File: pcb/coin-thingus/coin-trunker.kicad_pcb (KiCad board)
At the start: 2 copper layers, 65 x 80.5 mm, 69 parts, among them J1 6P6C, J2 6P6C, J3 Conn_02x20_Odd_Even, J4 Barrel_Jack_Switch_MountingPin, J5 Screw_Terminal_01x02, J6 Conn_01x05, J7 USB_B_Micro, K1 AGQ200A4, K2 AGQ200A4, K3 AGQ200A4, K4 AGQ200A4, Q1 BSS123L, T1 Sumida-13324-TO86, U1 ULN2003LV, U2 LT8304, U3 H11AA1, U4 TCA9534, U5 ILD74, U6 MCP1703A-3302_SOT23, U7 STM32F042F6Px

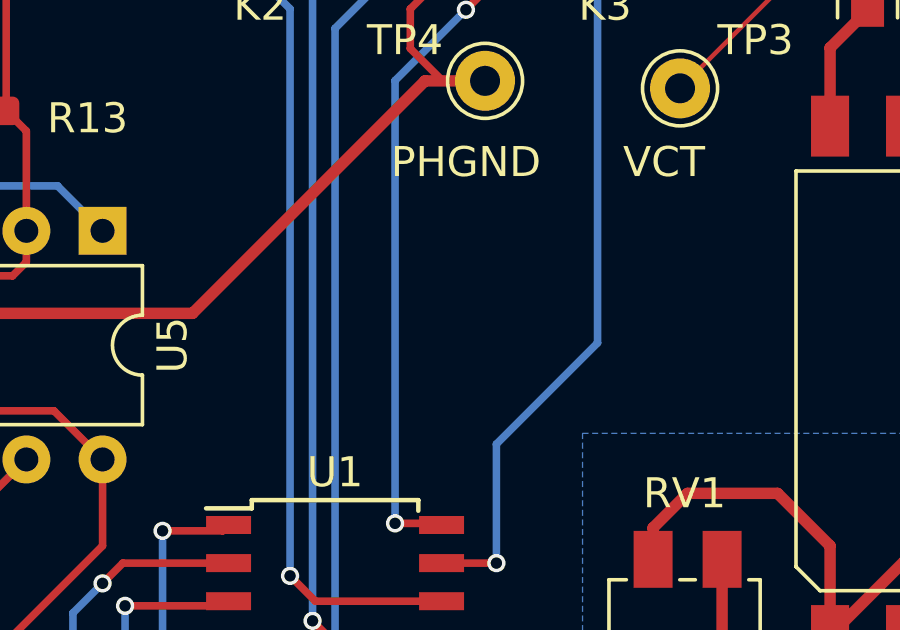
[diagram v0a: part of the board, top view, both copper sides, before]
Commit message: Add CERN-OHL-W v2 license
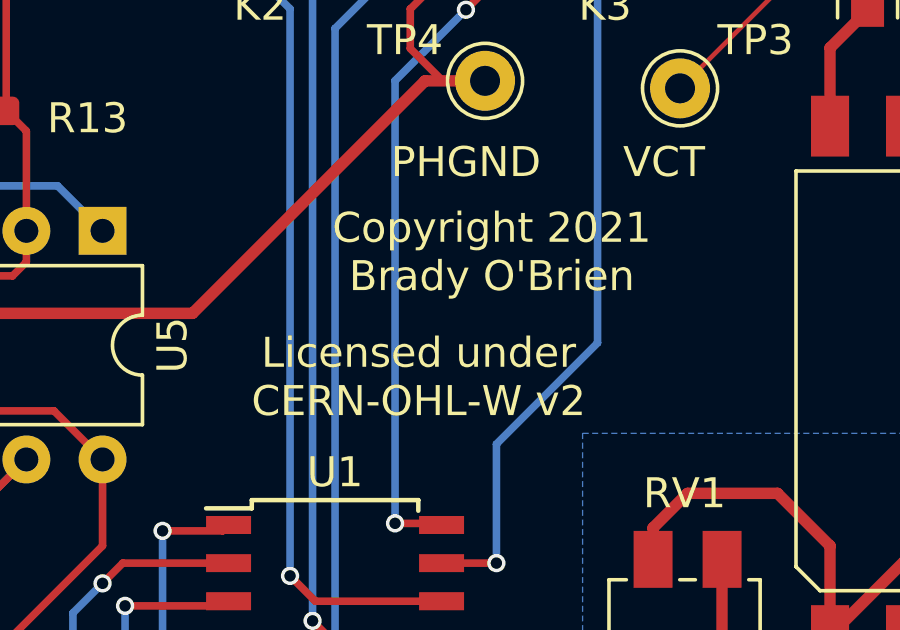
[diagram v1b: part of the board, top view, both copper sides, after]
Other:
- board text added: "Copyright 2021 Brady O'Brien"
- board text added: "Licensed under CERN-OHL-W v2"

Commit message: Some work towards v0.2
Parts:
- removed G***: LOGO, coin-trunker:phone_image
- removed JP1: SolderJumper_2_Open, Jumper:SolderJumper-2_P1.3mm_Open_Pad1.0x1.5mm
- added SW1: SW_SPST, Button_Switch_SMD:SW_SPST_TL3342, F.Cu at (126.3, 83.6)
- added U8: LTV-217, Package_SO:SOP-4_4.4x2.6mm_P1.27mm, F.Cu at (147.3, 67.6)
- K1, K2, K3: value AGQ200A4 -> HFD4/5-S
- R10, R7: footprint Resistor_SMD:R_0612_1632Metric -> Resistor_SMD:R_1206_3216Metric
- U1: footprint Package_SO:SOIC-16W_5.3x10.2mm_P1.27mm -> Package_SO:SOIC-16_3.9x9.9mm_P1.27mm
- U3: value H11AA1 -> LTV-217; footprint Package_DIP:DIP-6_W7.62mm -> Package_SO:SOP-4_4.4x2.6mm_P1.27mm
- U5: value ILD74 -> LTV-217; footprint Package_DIP:DIP-8_W7.62mm -> Package_SO:SOP-4_4.4x2.6mm_P1.27mm
- moved K4 107.9 mm to (181.2, 59.8), turned to 0 degrees
- moved R10 102.7 mm to (157.6, 55.6), turned to 0 degrees
- moved R7 98.6 mm to (178.0, 67.2), turned to 0 degrees
- moved K3 96.1 mm to (170.8, 59.8), turned to 0 degrees
- moved K2 86.5 mm to (149.7, 59.8), turned to 0 degrees
- moved U3 83.0 mm to (170.4, 67.6), turned to 0 degrees
- moved K1 78.6 mm to (139.3, 59.8), turned to 0 degrees
- moved U1 72.4 mm to (138.3, 71.2)
- moved U5 68.6 mm to (126.3, 73.1), turned to 0 degrees
- moved J4 50.6 mm to (127.1, 56.3)
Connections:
- K1 pad 5: Net-(K1-Pad5) -> /T_COIN
- K1 pad 7: /T_COIN -> Net-(K1-Pad7)
- K2 pad 2: Net-(K1-Pad4) -> Net-(K1-Pad2)
- K2 pad 7: Net-(K1-Pad5) -> Net-(K1-Pad7)
- U3 pad 3: Net-(U3-Pad3) -> GND
- U3 pad 4: GND -> /COIN_TEST
- U5 pad 3: Net-(J2-Pad4) -> GND
- U5 pad 4: /T_CO -> /OFF_HOOK_F
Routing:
- net GND: track 370.0 -> 0.00 mm, vias 11 -> 0
- net /5VRPI: track 117.8 -> 0.00 mm, vias 1 -> 0
- net /COIN_TEST: track 104.3 -> 0.00 mm, vias 1 -> 0
- net /3V3RPI: track 91.6 -> 0.00 mm, vias 1 -> 0
- net /5V: track 85.0 -> 0.00 mm, vias 5 -> 0
- net /SCL: track 78.7 -> 0.00 mm, vias 3 -> 0
- net /SDA: track 77.8 -> 0.00 mm, vias 3 -> 0
- net /48V: track 55.8 -> 0.00 mm
- net Earth: track 51.3 -> 0.00 mm
- net /3V3: track 50.8 -> 0.00 mm, vias 6 -> 0
- net Net-(D2-Pad2): track 49.8 -> 0.00 mm, vias 2 -> 0
- net /3V3USB: track 48.7 -> 0.00 mm, vias 6 -> 0
- net /FXS_TO_COIN_1: track 42.6 -> 0.00 mm, vias 2 -> 0
- net /HV_N: track 42.0 -> 0.00 mm, vias 2 -> 0
- net /5VUSB: track 39.8 -> 0.00 mm, vias 2 -> 0
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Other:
- board text added: "Coin Thingus v0.2"
- board text removed: "Coin Thingus v0.1"

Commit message: HV test board; A bunch of work towards v0.2
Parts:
- added C12: .1u, Capacitor_SMD:C_1210_3225Metric, F.Cu at (133.9, 69.7)
- added D10: LED, LED_SMD:LED_0603_1608Metric, F.Cu at (117.8, 60.6)
- added D11: LED, LED_SMD:LED_0603_1608Metric, F.Cu at (113.8, 65.8)
- added D12: LED, LED_SMD:LED_0603_1608Metric, F.Cu at (117.8, 63.2)
- added D13: D_TVS_x2_AAC, Package_TO_SOT_SMD:SOT-23, F.Cu at (133.3, 61.6)
- added D14: LED, LED_SMD:LED_0603_1608Metric, F.Cu at (137.6, 60.6)
- added D7: LED, LED_SMD:LED_0603_1608Metric, F.Cu at (113.8, 60.6)
- added D9: LED, LED_SMD:LED_0603_1608Metric, F.Cu at (113.8, 63.2)
- added Q2: BSS123L, Package_TO_SOT_SMD:SOT-23, F.Cu at (43.2, 89.5)
- added Q3: BSS123L, Package_TO_SOT_SMD:SOT-23, F.Cu at (43.2, 85.8)
- added R21: 470, Resistor_SMD:R_0603_1608Metric, F.Cu at (121.8, 60.6)
- added R22: 470, Resistor_SMD:R_0603_1608Metric, F.Cu at (117.8, 65.7)
- added R23: 470, Resistor_SMD:R_0603_1608Metric, F.Cu at (121.8, 63.1)
- added R24: 470, Resistor_SMD:R_0603_1608Metric, F.Cu at (125.8, 60.6)
- added R25: 470, Resistor_SMD:R_0603_1608Metric, F.Cu at (121.8, 65.7)
- added R26: 470, Resistor_SMD:R_0603_1608Metric, F.Cu at (137.5, 63.1)
- D8: footprint Diode_SMD:D_SMA -> Diode_SMD:D_SOD-323_HandSoldering
- J5: value Screw_Terminal_01x02 -> Screw_Terminal_01x01; footprint TerminalBlock_Phoenix:TerminalBlock_Phoenix_MPT-0,5-2-2.54_1x02_P2.54mm_Horizontal -> coin-trunker:screw_block_m3_5x7
- R7: footprint Resistor_SMD:R_1206_3216Metric -> Resistor_SMD:R_2010_5025Metric
- moved K4 110.1 mm to (73.2, 38.0), turned to 180 degrees
- moved R10 104.1 mm to (54.0, 45.5), turned to 90 degrees
- moved K3 98.0 mm to (73.2, 50.5), turned to 180 degrees
- moved R7 96.4 mm to (87.5, 34.0)
- moved U8 89.9 mm to (57.5, 67.5), turned to 270 degrees
- moved K2 89.4 mm to (60.8, 50.5), turned to 180 degrees
- moved U3 86.4 mm to (92.7, 29.8), turned to 180 degrees
- moved K1 81.5 mm to (60.8, 38.0), turned to 180 degrees
- moved U1 75.1 mm to (63.5, 77.0)
- moved U5 72.6 mm to (54.0, 67.5), turned to 270 degrees
- moved SW1 63.8 mm to (63.8, 95.8), turned to 180 degrees
- moved J4 50.4 mm to (91.5, 92.0)
- moved TP1 14.0 mm to (83.8, 45.0)
- moved TP2 12.0 mm to (97.2, 47.0)
- moved D8 10.7 mm to (93.8, 34.2)
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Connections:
- T1 pad 10: /HV_N -> Net-(D3-Pad2)
- T1 pad 6: Net-(D3-Pad2) -> /HV_N
- U7 pad 2: /SDA -> Net-(Q2-Pad2)
- U7 pad 3: /SCL -> Net-(Q3-Pad2)
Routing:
- net GND: track 0.00 -> 267.7 mm, vias 0 -> 5
- net /3V3USB: track 0.00 -> 64.8 mm, vias 0 -> 2
- net Earth: track 0.00 -> 55.4 mm, vias 0 -> 2
- net /3V3: track 0.00 -> 51.3 mm, vias 0 -> 4
- net /T_COIN: track 0.00 -> 46.8 mm
- net /5VUSB: track 0.00 -> 38.7 mm, vias 0 -> 4
- net Net-(K3-Pad2): track 0.00 -> 29.0 mm, vias 0 -> 2
- net /T_CO: track 0.00 -> 27.4 mm
- net /USB Controller Interface/SWDIO: track 0.00 -> 24.7 mm, vias 0 -> 2
- net /USB Controller Interface/SWCLK: track 0.00 -> 23.4 mm, vias 0 -> 3
- net /USB Controller Interface/NRST: track 0.00 -> 22.0 mm, vias 0 -> 2
- net /R_CO: track 0.00 -> 19.3 mm, vias 0 -> 2
- net Net-(K1-Pad7): track 0.00 -> 17.6 mm
- net /HV_EN_LV: track 0.00 -> 17.4 mm, vias 0 -> 2
- net Net-(J2-Pad4): track 0.00 -> 16.3 mm
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- removed copper zone on B.Cu, net GND
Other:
- board text added: "Bzzzzz"
- board text added: "High Voltage Very Danger"
- board text added: "Phone Here"
- board text added: "clicky"
- board text added: "control"
- board text removed: "To Phone"

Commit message: Bunch'o work towards v0.2
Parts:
- removed RV1: 100K, Potentiometer_SMD:Potentiometer_Bourns_3224X_Vertical
- removed TP4: TestPoint, Connector_Pin:Pin_D1.0mm_L10.0mm
- added C13: 1uF, Capacitor_SMD:C_0603_1608Metric, F.Cu at (59.2, 85.4)
- added C14: 270pF, Capacitor_SMD:C_0603_1608Metric, F.Cu at (43.8, 81.1)
- added C15: 270pF, Capacitor_SMD:C_0603_1608Metric, F.Cu at (43.8, 82.7)
- added D15: 1N4148WS, Diode_SMD:D_SOD-323_HandSoldering, F.Cu at (64.0, 87.8)
- added G***: LOGO, coin-trunker:phone_image, B.Cu at (62.0, 82.2)
- added JP1: SolderJumper_2_Open, Jumper:SolderJumper-2_P1.3mm_Open_TrianglePad1.0x1.5mm, B.Cu at (43.8, 40.0)
- added JP2: SolderJumper_2_Open, Jumper:SolderJumper-2_P1.3mm_Open_TrianglePad1.0x1.5mm, B.Cu at (43.8, 36.2)
- added Q4: BSS84, Package_TO_SOT_SMD:SOT-23, F.Cu at (67.4, 87.8)
- added R27: 10k, Resistor_SMD:R_0603_1608Metric, F.Cu at (71.0, 87.8)
- added R28: 500k, Resistor_SMD:R_0603_1608Metric, F.Cu at (62.0, 87.8)
- added R29: 10k, Resistor_SMD:R_0603_1608Metric, F.Cu at (41.2, 89.8)
- added R30: 10k, Resistor_SMD:R_0603_1608Metric, F.Cu at (41.2, 86.5)
- R3: value 100k -> 130k
- R7: value 3600R 2W -> 3.6K
- moved D13 90.4 mm to (48.7, 93.3), turned to 90 degrees
- moved D14 67.5 mm to (72.5, 78.5)
- moved R26 63.7 mm to (75.8, 78.5)
- moved R24 52.1 mm to (75.8, 75.0)
- moved R25 47.3 mm to (75.8, 76.8)
- moved D12 47.3 mm to (72.5, 76.8)
- moved R23 47.2 mm to (75.8, 73.3)
- moved D10 47.1 mm to (72.5, 73.3)
- moved R21 47.0 mm to (75.8, 69.8)
- moved C12 46.4 mm to (92.2, 49.4), turned to 180 degrees
- moved R3 45.4 mm to (88.3, 40.5), turned to 270 degrees
- moved R22 42.4 mm to (75.8, 71.5)
- moved D11 42.3 mm to (72.5, 75.0)
- moved D7 42.3 mm to (72.5, 69.8)
- moved D9 42.1 mm to (72.5, 71.5)
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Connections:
- C12 pad 1: /HV_P -> /HV_N
- C12 pad 2: /HV_N -> /HV_P
- R3 pad 1: Net-(R3-Pad1) -> /HV_N
- R3 pad 2: Net-(R3-Pad2) -> /HV_P
- R5 pad 2: Net-(R3-Pad2) -> Net-(R5-Pad2)
- R6 pad 1: Net-(R6-Pad1) -> Net-(D2-Pad2)
- T1 pad 10: Net-(D3-Pad2) -> /HV_N
- T1 pad 3: /48V -> Net-(D2-Pad2)
- T1 pad 5: Net-(D2-Pad2) -> /48V
- T1 pad 6: /HV_N -> Net-(D3-Pad2)
- U1 pad 2: /COIN_TEST_RELAY_LV -> /CT_LV_L
- U2 pad 7: Net-(R3-Pad2) -> Net-(R5-Pad2)
- U2 pad 8: Net-(R3-Pad1) -> Net-(U2-Pad8)
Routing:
- net /5VRPI: track 2.54 -> 105.4 mm, vias 0 -> 6
- net /5V: track 13.7 -> 116.2 mm, vias 0 -> 10
- net /COIN_TEST: track 5.21 -> 99.0 mm, vias 0 -> 4
- net /3V3RPI: track 0.00 -> 91.8 mm, vias 0 -> 6
- net GND: track 267.7 -> 350.8 mm, vias 5 -> 12
- net /SDA: track 13.9 -> 74.8 mm, vias 0 -> 7
- net /SCL: track 10.5 -> 67.6 mm, vias 0 -> 5
- net /48V: track 0.00 -> 56.0 mm, vias 0 -> 2
- net /FXS_TO_COIN_1: track 0.00 -> 48.2 mm, vias 0 -> 2
- net /HV_N: track 8.82 -> 54.9 mm, vias 0 -> 1
- net /COIN_TEST_RELAY: track 0.00 -> 39.8 mm, vias 0 -> 4
- net /CO_HOLD: track 0.00 -> 30.9 mm, vias 0 -> 2
- net Net-(D5-Pad1): track 14.6 -> 41.8 mm, vias 0 -> 2
- net Net-(R26-Pad2): track 0.00 -> 26.0 mm, vias 0 -> 4
- net Earth: track 55.4 -> 80.7 mm
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- added copper zone on F.Cu, net /48V
- added copper zone on F.Cu, net /HV_N
- added copper zone on F.Cu, net /HV_P
- added copper zone on B.Cu, net GND
- added copper zone on F.Cu, net GND
- added copper zone on F.Cu, net Net-(D2-Pad2)
- added copper zone on F.Cu, net Net-(D3-Pad2)
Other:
- rule trace_min: 0.1524 -> 0.127
- board text added: "24-56v seems to work"
- board text added: "5V"
- board text added: "BLINK"
- board text added: "Blinkinlights"
- board text added: "COINO"
- board text added: "CPOL"
- board text added: "CTEST"
- board text added: "HOLD"
- board text added: "tah-duh-da"
- board text removed: "48-ish V maybe less"
- board text removed: "PHGND"

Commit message: Coin thing v0.2 PCB
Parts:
- R6: value 260k -> 240k
- moved D6 27.4 mm to (38.9, 78.5), turned to 180 degrees
- moved G*** 4.20 mm to (66.2, 82.3)
- moved J4 1.50 mm to (89.7, 90.9)
- moved R9 0.56 mm to (44.3, 76.4)
- moved C1 0.30 mm to (88.1, 86.6)
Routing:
- net /5VRPI: track 105.4 -> 72.9 mm, vias 6 -> 2
- net /5V: track 116.2 -> 142.8 mm, vias 10 -> 9
- net GND: track 350.8 -> 357.4 mm
- net Net-(R26-Pad2): track 26.0 -> 30.7 mm, vias 4 -> 2
- net Net-(J2-Pad4): track 16.2 -> 19.2 mm
- net /3V3RPI: track 91.8 -> 94.3 mm, vias 6 -> 4
- net /USB Controller Interface/SWCLK: track 25.4 -> 27.8 mm, vias 2 -> 1
- net /48V: track 56.0 -> 53.9 mm
- net /FXS_TO_COIN_1: track 48.2 -> 46.2 mm
- net /HV_EN: track 12.9 -> 14.9 mm
- net /5VUSB: track 32.3 -> 30.4 mm
- net /COIN_TEST: track 99.0 -> 97.4 mm
- net /CO_HOLD: track 30.9 -> 29.7 mm
- net Net-(Q1-Pad1): track 16.1 -> 15.0 mm
- net /USB Controller Interface/SWDIO: track 27.7 -> 26.7 mm, vias 2 -> 0
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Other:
- net class HVSide added: clearance 0.1524, trace_width 0.2032, via_dia 0.6096, via_drill 0.381
- board text added: "Blinkenlights"
- board text added: "CL"
- board text added: "Coin Thing v0.2"
- board text added: "DI"
- board text added: "GN"
- board text added: "RS"
- board text added: "VI"
- board text added: "brain"
- board text added: "co-brain"
- board text added: "tuh-duh-da"
- board text removed: "Blinkinlights"
- board text removed: "Coin Thingus v0.2"
- board text removed: "control"
- board text removed: "tah-duh-da"

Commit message: Start work on alternate micro
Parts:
- removed G***: LOGO, coin-trunker:phone_image
- removed U7: STM32F042F6Px, Package_SO:TSSOP-20_4.4x6.5mm_P0.65mm
- added U9: STM32F042K6Tx, Package_QFP:LQFP-32_7x7mm_P0.8mm, F.Cu at (54.6, 87.6)
- D3: value CMMR1U-06 -> CMMR1U-06 / 1N4007W
- J7: footprint Connector_USB:USB_Micro-B_Molex-105017-0001 -> coin-trunker:USB_Micro-B_Molex-105017-0001
- K4: value AGQ200A4 -> HFD4/5-S
- R1, R11, R12, R13, R14, R15, R16, R17, R18, R19, R2, R20, R21, R22, R23, R24, R25, R26, R27, R28, R29, R3, R30, R4, R5, R9: footprint Resistor_SMD:R_0603_1608Metric -> Resistor_SMD:R_0402_1005Metric
- SW1: value SW_SPST -> TS-1187A-C-E-B
- U2: value LT8304 -> LT8304-1
- moved C13 4.65 mm to (63.8, 84.7)
- moved R17 4.44 mm to (61.4, 91.5)
- moved R11 3.21 mm to (56.2, 80.0)
- moved R12 3.21 mm to (56.2, 78.5)
- moved R14 3.21 mm to (56.2, 77.0)
- moved C10 2.53 mm to (47.9, 84.2)
- moved R28 2.31 mm to (64.3, 88.0)
- moved D15 2.22 mm to (66.2, 88.1)
- moved Q4 1.71 mm to (69.1, 88.0)
- moved C5 1.35 mm to (50.4, 81.0)
- moved R27 1.00 mm to (71.6, 88.6), turned to 270 degrees
- moved D6 0.95 mm to (39.2, 79.4)
- moved U4 0.85 mm to (50.3, 77.0)
- moved R19 0.82 mm to (44.4, 77.4)
- moved Q2 0.52 mm to (43.5, 89.6)
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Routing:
- net GND: track 357.4 -> 168.8 mm, vias 12 -> 0
- net /3V3USB: track 80.4 -> 0.00 mm
- net /5V: track 142.8 -> 70.6 mm, vias 9 -> 5
- net /3V3: track 70.1 -> 0.00 mm, vias 4 -> 0
- net Net-(R26-Pad2): track 30.7 -> 0.00 mm, vias 2 -> 0
- net /5VUSB: track 30.4 -> 0.00 mm, vias 2 -> 0
- net /USB Controller Interface/SWCLK: track 27.8 -> 0.00 mm, vias 1 -> 0
- net /USB Controller Interface/SWDIO: track 26.7 -> 0.00 mm
- net /SDA: track 75.4 -> 49.3 mm, vias 6 -> 2
- net /3V3RPI: track 94.3 -> 68.8 mm, vias 4 -> 1
- net /USB Controller Interface/NRST: track 24.2 -> 0.00 mm
- net /CT_LV_L: track 21.3 -> 0.00 mm
- net /SCL: track 68.2 -> 48.1 mm, vias 5 -> 1
- net /USB Controller Interface/BOOT0: track 19.5 -> 0.00 mm, vias 2 -> 0
- net /HV_EN_LV: track 18.1 -> 0.00 mm, vias 2 -> 0
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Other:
- board text added: "Chip Shortage Edition"
- board text added: "Coin Thing v0.2.1"
- board text removed: "Coin Thing v0.2"
